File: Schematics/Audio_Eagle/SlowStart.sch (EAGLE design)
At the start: 19 parts

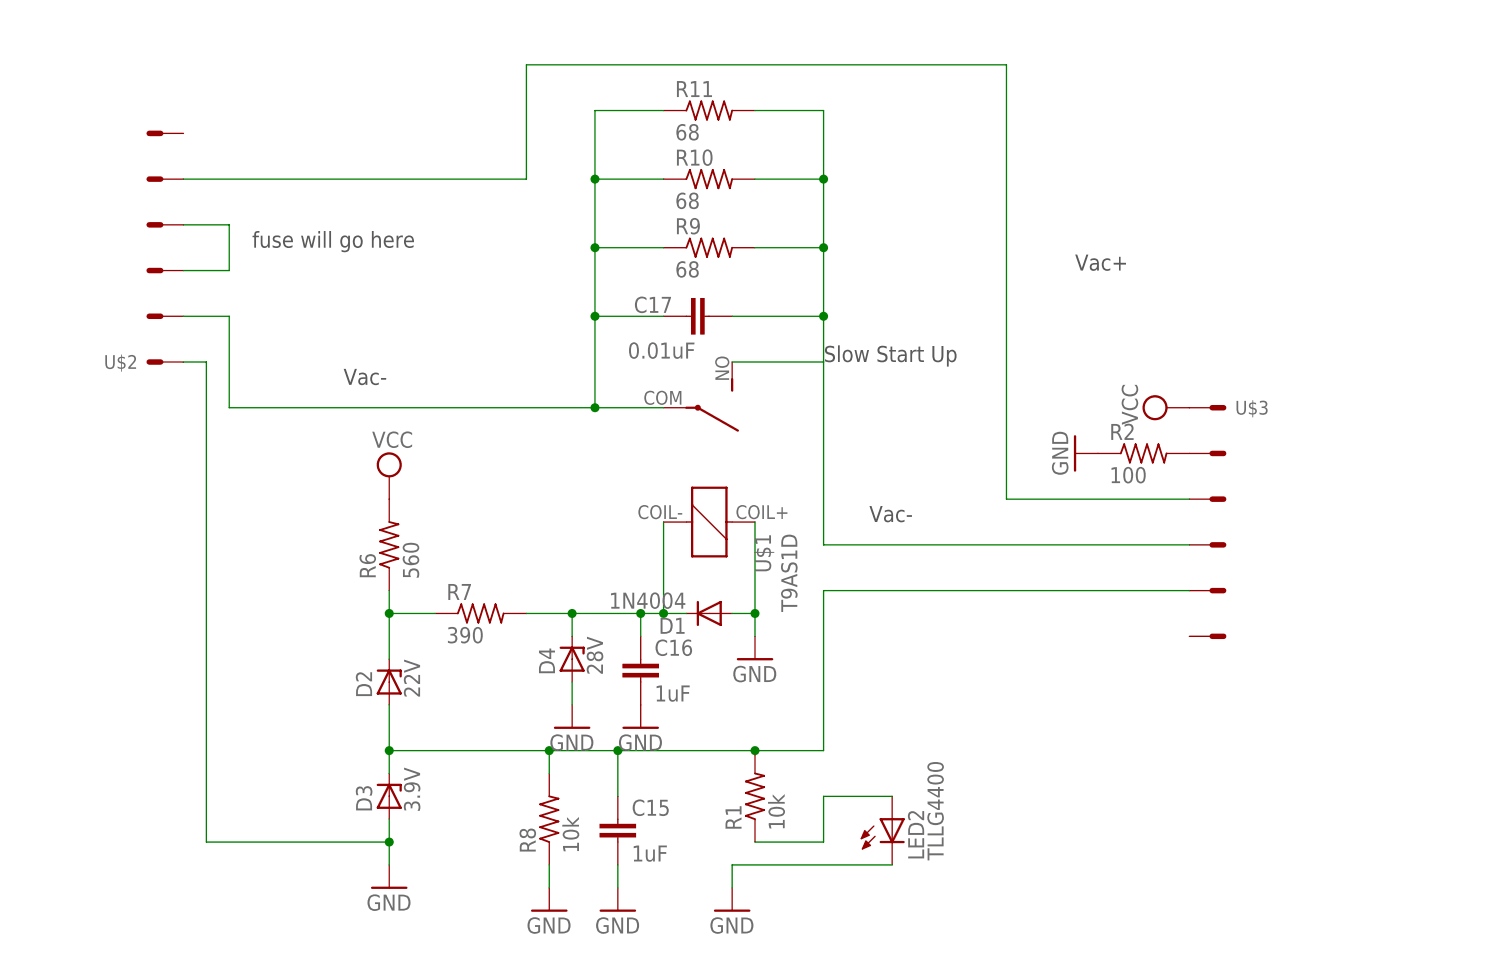
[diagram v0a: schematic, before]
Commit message: updated slow start
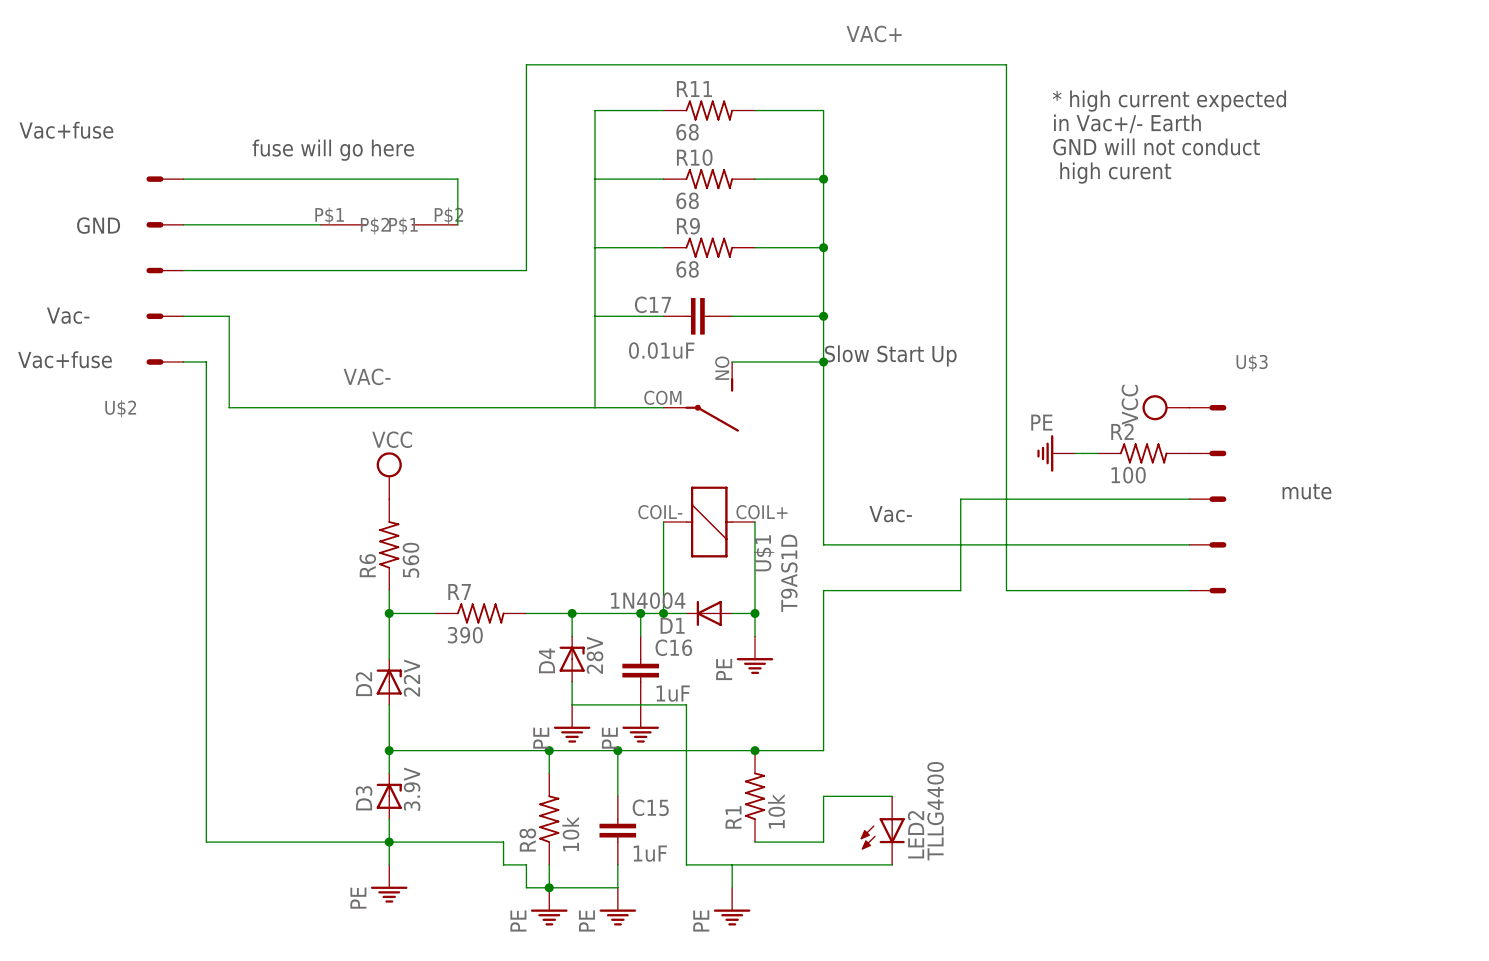
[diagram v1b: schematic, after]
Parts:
- added U$4: FUSE, Amplifier_Parts:FUSE
- U$2, U$3: value MOLEX_6P -> SCREW_TERMINAL_5; device Amplifier_Parts:MOLEX_6P -> Amplifier_Parts:SCREW_TERMINAL_5
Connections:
- removed net N$1 (its old number): U$2.S2, U$2.S3
- new net VAC+: U$2.S3, U$3.S5
- new net VAC-: C17.1, R10.1, R11.1, R9.1, U$1.COM, U$2.S2
- net GND: now also U$2.S1; no longer U$2.S
- net N$12: now also U$3.S3; no longer U$3.S4
- net N$2: now also U$2.S5, U$4.P$2; no longer U$2.S4, U$3.S2
- net N$3: now also R2.2, U$3.S2; no longer C17.1, R10.1, R11.1, R9.1, U$1.COM, U$2.S1
- net N$5: now also U$2.S4, U$4.P$1; no longer R2.2, U$3.S1
- net N$8: now also U$3.S4; no longer U$3.S3
- net VCC: no longer U$3.S
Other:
- note added: "* high current expected in Vac+/- Earth GND will not conduct high curent"
- note added: "GND"
- note added: "Vac+fuse"
- note added: "mute"
- note removed: "Vac+"

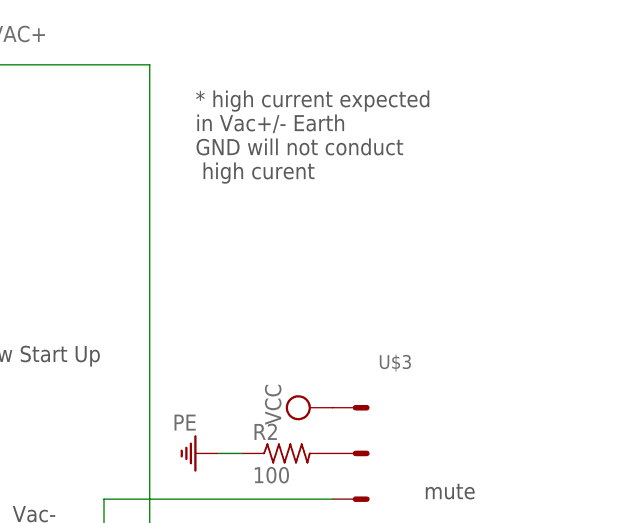
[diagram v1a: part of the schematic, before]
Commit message: changes to slow start
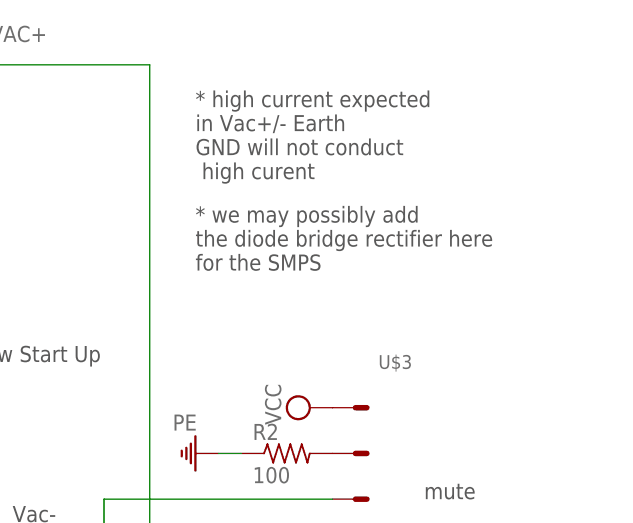
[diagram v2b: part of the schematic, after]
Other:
- note added: "* we may possibly add the diode bridge rectifier here for the SMPS"
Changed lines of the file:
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@@
 <text x="-36.1696" y="60.2996" size="1.778" layer="97">Vac+fuse</text>
 <text x="-36.0172" y="85.8012" size="1.778" layer="97">Vac+fuse</text>
+<text x="78.74" y="71.12" size="1.778" layer="97">* we may possibly add
+the diode bridge rectifier here
+for the SMPS</text>
 </plain>
 <instances>
